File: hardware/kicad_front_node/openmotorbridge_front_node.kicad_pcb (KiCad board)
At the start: 2 copper layers, 82 x 50 mm, 58 parts, among them J1 12V_KL15_GND, J10 12V_QI_POWER, J11 12V_AUX_LIGHT, J12 QWIIC_I2C, J2 CAN_H_L_GND, J3 HANDLEBAR_MULTI_BTN, J4 USB_UPSTREAM_HOST, J5 USB_DN1_PHONE_PD20W, J5_MP3 USB_DN3_GLOVEBOX_PD20W, J6 USB_DN2_CP2AA_PIGTAIL, J6_AUX USB_DN4_COCKPIT_AUX, J7 USB-C_SERVICE, J8 ACTION_CAM_5V_PWR, J9 MIRROR_BSD_LEDS, K1 CPC1017N_CAN_RELAY, Q1 DMN63D8_BSD_MOSFET, Q2 TPS1H100_AUX_LIGHT, SW1 BOOT, SW2 RESET, U1 ESP32-S3-WROOM-1U, U2 USB2514Bi-AEZG, U3 TPS54302_5V_BUCK, U4 TPS2051B_PORT2_GATE, U5 SW3526_USB_PD1_20W, U6 TCAN334G_CAN, U7 TLV75533P_3V3_LDO, U8 SW3526_USB_PD3_20W, U9 DW3110, Y1 24.000MHz

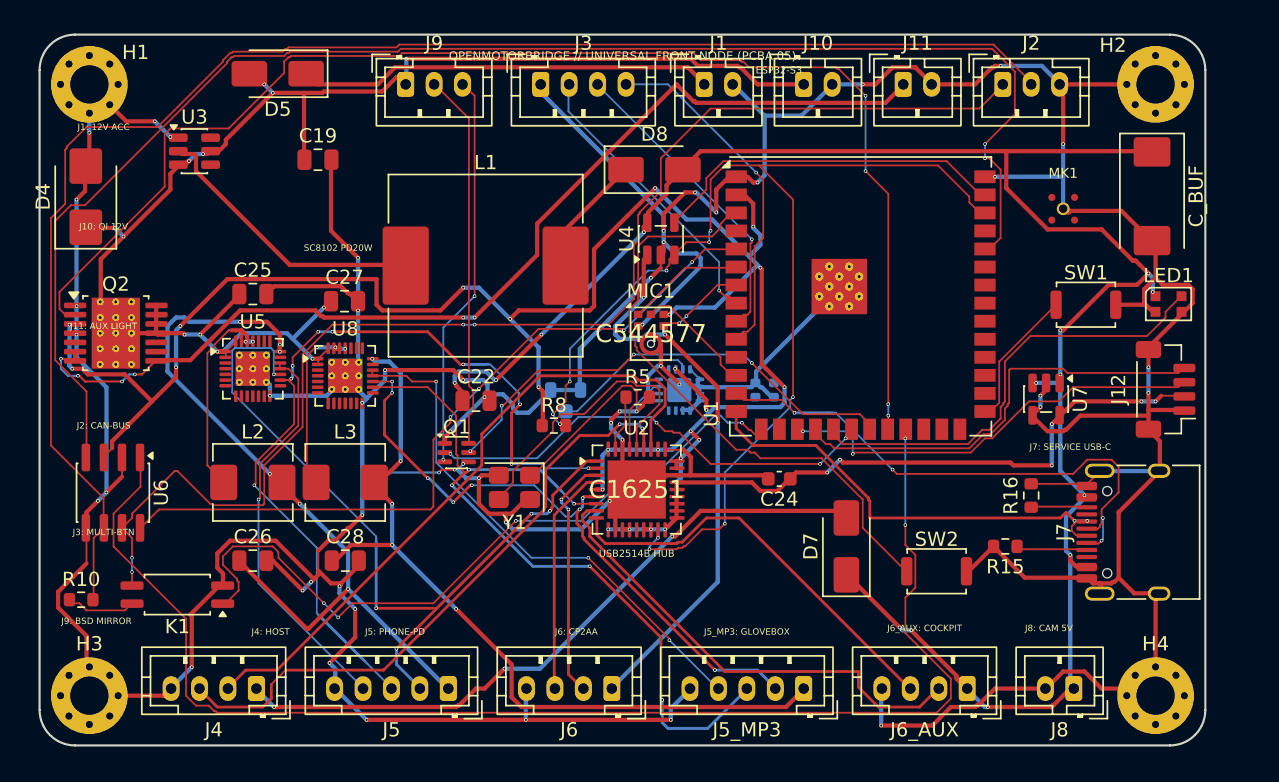
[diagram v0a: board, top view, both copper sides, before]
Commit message: fix(hardware): fleet-wide 7-PCBA remediation, schematic parity & doc alignment
- PCBA 01 (Central Box): Synchronized DTM-12 schematic and PCB routing, purged obsolete analog audio transformers/HD26 connector.
- PCBA 03 (Smart Cartridge): Verified Kelvin ground isolation on J_AUDIO_PWR, resolved U1.16 BAY_SELECT single net.
- PCBA 05 (Front Node): Mapped DW3110 UWB SPI/IRQ/RST to ESP32-S3 pads 30-35, connected MK1 I2S MEMS mic and Y_UWB crystal.
- PCBA 07 (Smart Keyfob): Connected 12 unrouted signals (SX1262 LoRa SPI, DRV2605L I2C, SWD, RTC crystal, buttons) to nRF52840 pads.
- PCBA 08 (Radar Sub-MCU): Synchronized J1.1 power rail to VCC_5V, connected Y1_UWB crystal to DW3110 pads 4 & 5.
- PCBA 09 & PCBA 10 (OMM 2.4 GHz & 446 MHz): Verified 4-layer stackup, BQ24075 ground ties, SA818 isolation, and vertical B.Cu J_HELMET orientation.
- Tools: Added verify_hardware_integrity.py with automated DRC/parity/single-net/floating-pad checks (all 7 PCBAs HEALTHY).
- Docs: Synchronized docs/de and docs/en hardware specifications, pinouts, and DTM-12 architecture.
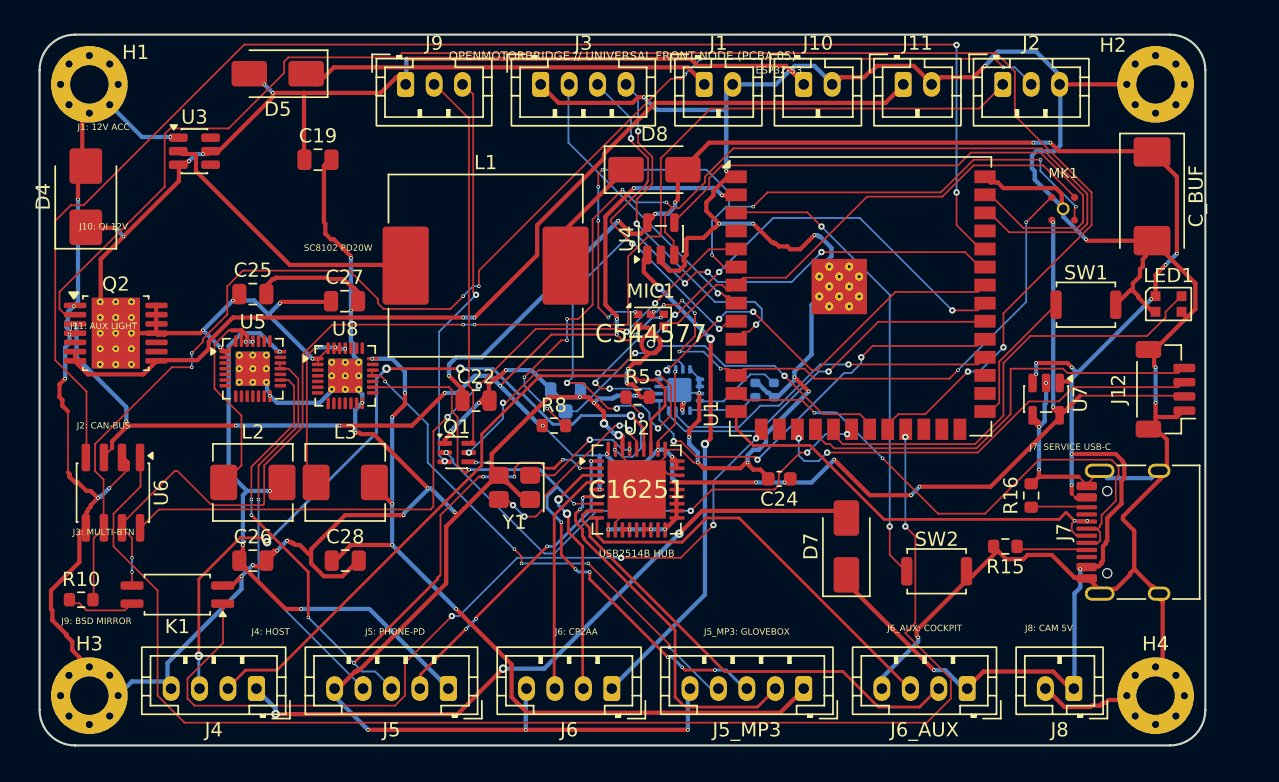
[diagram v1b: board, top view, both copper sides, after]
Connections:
- MK1 pad 1: (no net) -> MIC_I2S_DATA
- MK1 pad 2: (no net) -> MIC_I2S_BCLK
- MK1 pad 3: (no net) -> MIC_I2S_WS
- MK1 pad 4: (no net) -> VCC_3V3
- U1 pad 30: (no net) -> UWB_SCK
- U1 pad 31: (no net) -> UWB_MOSI
- U1 pad 32: (no net) -> UWB_MISO
- U1 pad 33: (no net) -> UWB_CS
- U1 pad 34: (no net) -> UWB_IRQ
- U1 pad 35: (no net) -> UWB_RST
- U1 pad 4: KL15_SENSE -> (no net)
- U2 pad 14: VDD12_HUB -> (no net)
- U3 pad 4: FB_BUCK -> (no net)
- U3 pad 6: BST_BUCK -> (no net)
- U9 pad 4: GND -> UWB_XTAL1
- U9 pad 5: GND -> UWB_XTAL2
- Y_UWB pad 1: (no net) -> UWB_XTAL1
- Y_UWB pad 3: (no net) -> UWB_XTAL2
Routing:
- net UWB_RST: track 0.00 -> 54.0 mm, vias 0 -> 7
- net MIC_I2S_WS: track 7.94 -> 58.5 mm, vias 0 -> 9
- net USB_DN1_DM: track 64.8 -> 21.8 mm, vias 5 -> 4
- net UWB_CS: track 0.00 -> 39.9 mm, vias 0 -> 5
- net MIC_I2S_DATA: track 7.95 -> 41.7 mm, vias 0 -> 8
- net MIC_I2S_BCLK: track 6.02 -> 34.9 mm, vias 2 -> 0
- net UWB_MOSI: track 0.00 -> 28.8 mm, vias 0 -> 3
- net UWB_IRQ: track 0.00 -> 28.3 mm, vias 0 -> 3
- net UWB_MISO: track 0.00 -> 26.4 mm, vias 0 -> 1
- net UWB_SCK: track 0.00 -> 24.5 mm, vias 0 -> 1
- net GND: track 465.5 -> 488.6 mm, vias 54 -> 55
- net AUX_LIGHT_EN: track 93.5 -> 114.8 mm, vias 4 -> 2
- net VCC_3V3: track 183.9 -> 164.1 mm, vias 31 -> 30
- net USB_DN3_DM: track 44.9 -> 26.2 mm, vias 8 -> 2
- net OTTOCAST_PWR_EN: track 24.8 -> 42.4 mm
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
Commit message: feat(hardware): achieve 100% 0-error DRC across all 7 official PCBAs and complete 4-layer Cartridge audio switching
- PCBA 01 (Central Box): Resolved keepout zone violation at U.FL ANT1, refilled zones (0 errors, 0 unconnected).
- PCBA 03 (Universal Smart Cartridge): Upgraded to 4 layers (JLC04161H), added SPDT analog/digital switch U4 (TS5A3159DBVR) on B.Cu and 10k pull-up R9 on F.Cu, routed symmetrical audio/OMM nets, schematic ERC 0 errors, DRC 0 errors, 0 unconnected.
- PCBA 05 (Front Node): 4-layer upgrade, solid GND plane, snapped OTTOCAST_FAULT_N (0 errors, 0 unconnected).
- PCBA 07 (Smart Keyfob): 4-layer upgrade, fixed Edge.Cuts arc alignment, routed U2 pad 23 (0 errors, 0 unconnected).
- PCBA 08 (Radar Sub-MCU), PCBA 09 (OMM 2.4 GHz), PCBA 10 (OMM 446 MHz): Verified 100% clean (0 errors, 0 unconnected).
- Added reproducibility tools: tools/sync_cartridge_sch.py and tools/remediate_pcba03.py.
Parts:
- moved Y1 4.21 mm to (129.4, 103.2), turned to 90 degrees
- turned U2 to 90 degrees
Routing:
- net GND: track 488.6 -> 100.6 mm, vias 55 -> 31
- net AUX_LIGHT_EN: track 114.8 -> 77.1 mm, vias 2 -> 6
- net CAN_L: track 94.4 -> 128.3 mm, vias 7 -> 3
- net USB_DN1_DM: track 21.8 -> 53.3 mm, vias 4 -> 1
- net UWB_RST: track 54.0 -> 29.3 mm, vias 7 -> 3
- net USB_DN3_DM: track 26.2 -> 49.4 mm, vias 2 -> 3
- net CAN_SILENT: track 53.3 -> 72.8 mm, vias 4 -> 2
- net MIC_I2S_WS: track 58.5 -> 40.2 mm, vias 9 -> 4
- net OTTOCAST_FAULT_N: track 72.5 -> 54.9 mm, vias 6 -> 7
- net USB_UP_DP: track 51.4 -> 34.1 mm, vias 5 -> 3
- net VCC_3V3: track 164.1 -> 149.0 mm, vias 30 -> 24
- net USB_UP_DM: track 46.3 -> 32.1 mm, vias 0 -> 1
- net CAN_TERM_EN: track 59.7 -> 45.5 mm, vias 4 -> 6
- net VCC_5V_OTTOCAST: track 35.5 -> 49.1 mm, vias 3 -> 0
- net UWB_CS: track 39.9 -> 27.5 mm, vias 5 -> 3
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- added copper zone on In1.Cu, net GND
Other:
- copper layers 2 -> 4

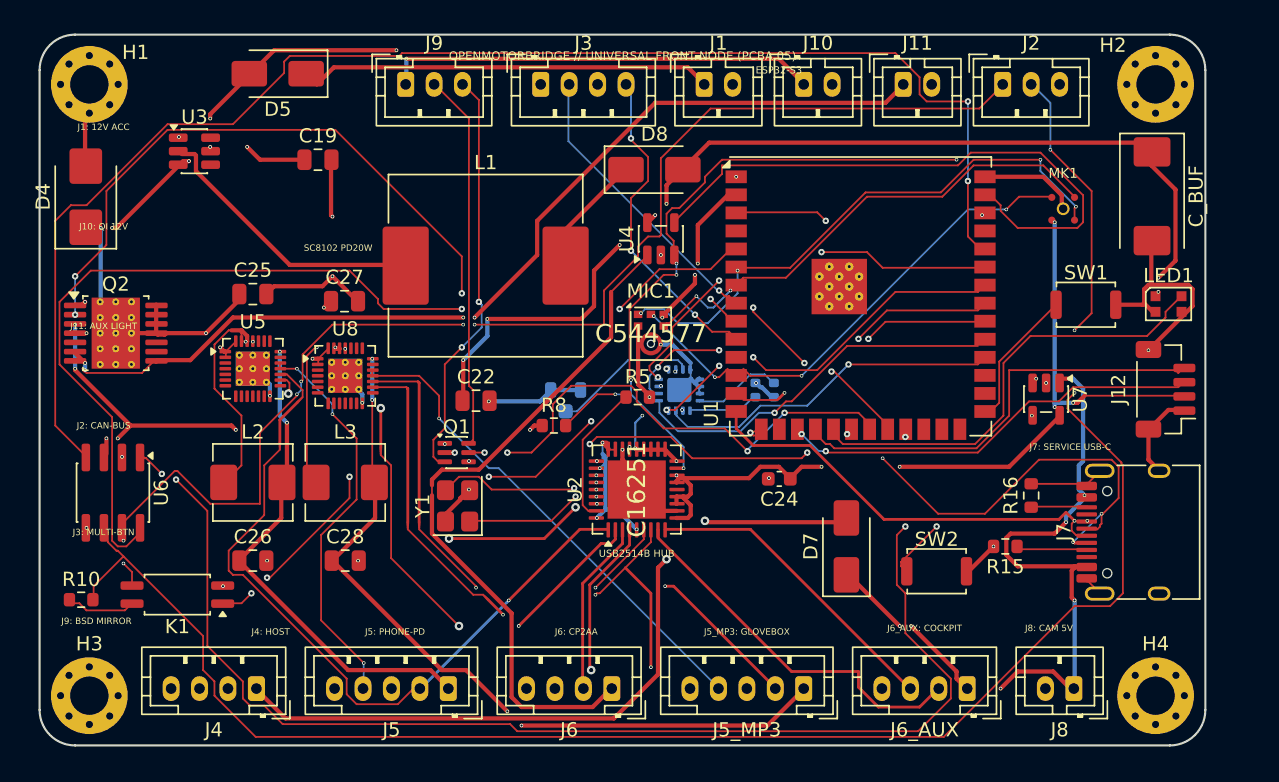
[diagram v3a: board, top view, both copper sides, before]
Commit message: feat(front-node): finalize dual-satellite architecture, CAD enclosures and smart-screen mode
- PCBA 05: Streamline board to 44 components with J_COCKPIT (16-pin) & J_VEHICLE (8-pin) dual-row headers, ESP32-S3 and DW3000 UWB.
- Enclosure: Update 00_front_node_tub.scad with continuous O-ring perimeter groove and circular Ø 8.0 mm TPU cable gland entries.
- Satellites: Implement cockpit_breakout_block.scad (5x USB-C, PTT, M3 clamp, dovetail) and vehicle_breakout_block.scad (4x COTS latching sockets).
- Use-Cases: Document 3 cockpit operating modes for RKS/naked cruisers including Mode C standalone smart-screen (Carpuride/Chigee) on [HOST].
- CAD & BOM: Re-render all Front Node 3D previews, register build targets in build_cad_from_openscad.py, and update doc chapters 07, 08, 15 & bom_catalog.js.
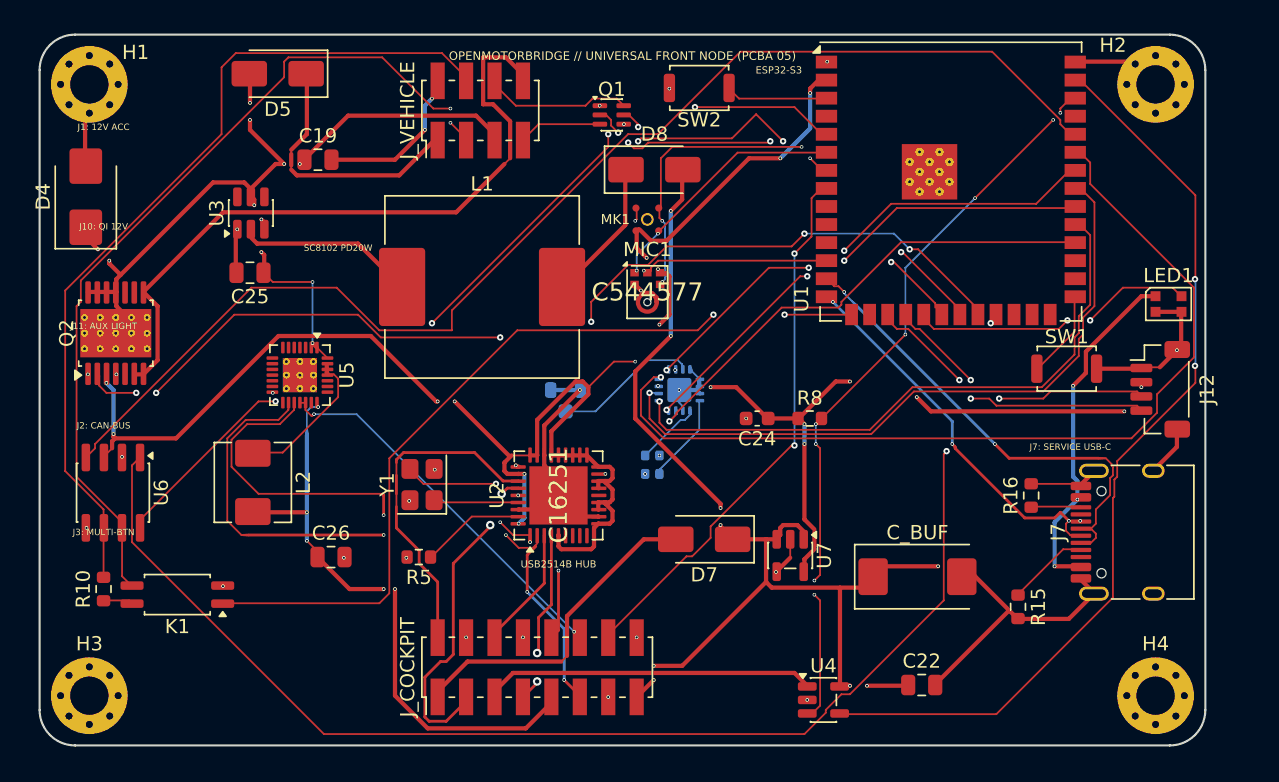
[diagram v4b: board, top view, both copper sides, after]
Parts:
- removed C27: 10uF_50V_PD3, C_0805_2012Metric
- removed C28: 22uF_25V_PD3, C_0805_2012Metric
- removed J1: 12V_KL15_GND, JST_PH_B2B-PH-K_1x02_P2.00mm_Vertical
- removed J10: 12V_QI_POWER, JST_PH_B2B-PH-K_1x02_P2.00mm_Vertical
- removed J11: 12V_AUX_LIGHT, JST_PH_B2B-PH-K_1x02_P2.00mm_Vertical
- removed J2: CAN_H_L_GND, JST_PH_B3B-PH-K_1x03_P2.00mm_Vertical
- removed J3: HANDLEBAR_MULTI_BTN, JST_PH_B4B-PH-K_1x04_P2.00mm_Vertical
- removed J4: USB_UPSTREAM_HOST, JST_PH_B4B-PH-K_1x04_P2.00mm_Vertical
- removed J5: USB_DN1_PHONE_PD20W, JST_PH_B5B-PH-K_1x05_P2.00mm_Vertical
- removed J5_MP3: USB_DN3_GLOVEBOX_PD20W, JST_PH_B5B-PH-K_1x05_P2.00mm_Vertical
- removed J6: USB_DN2_CP2AA_PIGTAIL, JST_PH_B4B-PH-K_1x04_P2.00mm_Vertical
- removed J6_AUX: USB_DN4_COCKPIT_AUX, JST_PH_B4B-PH-K_1x04_P2.00mm_Vertical
- removed J8: ACTION_CAM_5V_PWR, JST_PH_B2B-PH-K_1x02_P2.00mm_Vertical
- removed J9: MIRROR_BSD_LEDS, JST_PH_B3B-PH-K_1x03_P2.00mm_Vertical
- removed L3: 4.7uH_PD3_Choke, L_Sunlord_MWSA0503S
- removed U8: SW3526_USB_PD3_20W, QFN-28-1EP_4x4mm_P0.4mm_EP2.4x2.4mm_ThermalVias
- added J_COCKPIT: COCKPIT_16P_SMD, PinHeader_2x08_P2.00mm_Vertical_SMD, F.Cu at (135.0, 114.5)
- added J_VEHICLE: VEHICLE_8P_SMD, PinHeader_2x04_P2.00mm_Vertical_SMD, F.Cu at (131.0, 75.3)
- moved SW2 37.9 mm to (146.4, 73.8), turned to 180 degrees
- moved C22 37.2 mm to (162.1, 115.8)
- moved U4 34.4 mm to (155.1, 116.8), turned to 0 degrees
- moved C_BUF 31.4 mm to (161.8, 108.1), turned to 0 degrees
- moved MK1 29.3 mm to (142.8, 83.0)
- moved Q1 26.1 mm to (140.2, 75.7)
- moved U7 21.1 mm to (152.8, 106.6)
- moved R5 19.1 mm to (126.7, 106.8), turned to 180 degrees
- moved R8 18.0 mm to (154.2, 97.0)
- moved U1 10.3 mm to (164.1, 80.3)
- moved D7 10.0 mm to (146.8, 105.5), turned to 180 degrees
- moved Y_UWB 9.49 mm to (143.1, 100.2), turned to 90 degrees
- moved U3 5.89 mm to (114.9, 82.5), turned to 90 degrees
- moved U2 5.52 mm to (136.5, 102.4)
- moved C26 5.51 mm to (120.5, 106.8)
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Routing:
- net CAN_L: track 128.3 -> 60.2 mm, vias 3 -> 0
- net VBUS_PD3_OUT: track 54.7 -> 0.00 mm, vias 4 -> 0
- net USB_DN3_DP: track 50.3 -> 0.00 mm, vias 3 -> 0
- net USB_DN3_DM: track 49.4 -> 0.00 mm, vias 3 -> 0
- net UWB_RST: track 29.3 -> 64.6 mm, vias 3 -> 1
- net USB_DN3_CC: track 34.9 -> 0.00 mm, vias 1 -> 0
- net +12V_PROT: track 100.8 -> 68.1 mm, vias 12 -> 11
- net USB_UP_VBUS: track 52.7 -> 23.3 mm, vias 2 -> 0
- net CAN_H: track 89.9 -> 60.7 mm, vias 6 -> 2
- net ESP_EN: track 35.8 -> 7.30 mm, vias 2 -> 0
- net VCC_5V: track 138.4 -> 110.8 mm, vias 15 -> 12
- net USB_DN4_DM: track 26.4 -> 0.00 mm
- net VCC_5V_OTTOCAST: track 49.1 -> 23.4 mm
- net BSD_RIGHT_N: track 29.1 -> 5.86 mm, vias 2 -> 0
- net PTT_IN3_N: track 22.8 -> 0.00 mm, vias 3 -> 0
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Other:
- board text removed: "J4: HOST"
- board text removed: "J5: PHONE-PD"
- board text removed: "J5_MP3: GLOVEBOX"
- board text removed: "J6: CP2AA"
- board text removed: "J6_AUX: COCKPIT"
- board text removed: "J8: CAM 5V"
- board text removed: "J9: BSD MIRROR"

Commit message: feat(front-node): integrate I2C bus into J_VEHICLE 12-pin, pass prefab-gate & update cad packages
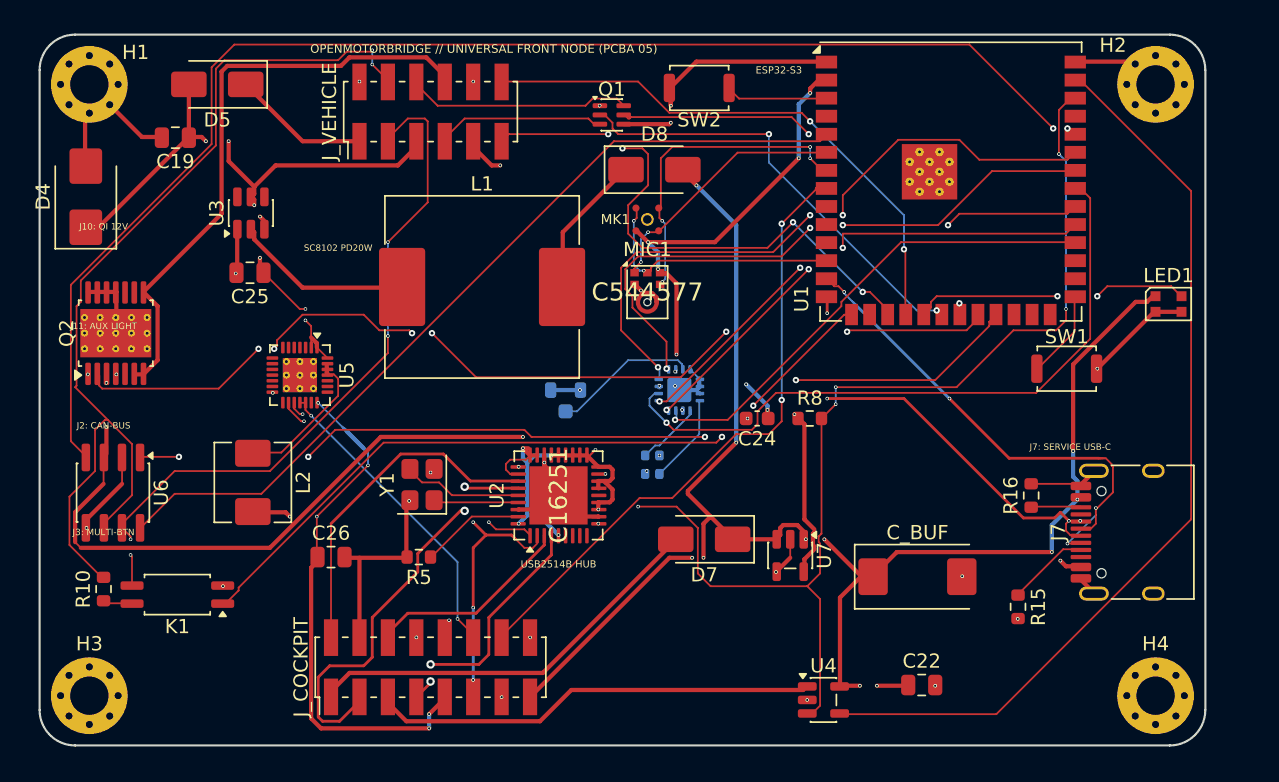
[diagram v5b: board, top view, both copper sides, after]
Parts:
- removed J12: QWIIC_I2C, JST_SH_BM04B-SRSS-TB_1x04-1MP_P1.00mm_Vertical
- removed the J_VEHICLE at (131.0, 75.3)
- added J_VEHICLE: VEHICLE_12P_SMD, PinHeader_2x06_P2.00mm_Vertical_SMD, F.Cu at (127.5, 75.4)
- moved C19 10.1 mm to (109.5, 77.2), turned to 180 degrees
- moved J_COCKPIT 7.50 mm to (127.5, 114.5)
- moved D5 4.32 mm to (112.5, 73.5)
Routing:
- net TWAI_TX: track 94.7 -> 65.0 mm, vias 2 -> 4
- net I2C_SCL: track 20.4 -> 39.3 mm
- net I2C_SDA: track 20.9 -> 39.6 mm, vias 2 -> 4
- net UWB_RST: track 64.6 -> 46.3 mm, vias 1 -> 3
- net VCC_3V3: track 169.7 -> 154.2 mm
- net USB_DN1_DP: track 46.6 -> 33.9 mm
- net CAN_H: track 60.7 -> 49.5 mm, vias 2 -> 4
- net OTTOCAST_FAULT_N: track 68.3 -> 79.4 mm, vias 9 -> 6
- net USB_DN1_DM: track 39.7 -> 30.5 mm, vias 4 -> 3
- net KL15_12V_SW: track 18.7 -> 9.66 mm
- net TWAI_RX: track 87.5 -> 96.0 mm, vias 0 -> 2
- net UWB_MOSI: track 43.4 -> 35.0 mm, vias 1 -> 3
- net UWB_IRQ: track 34.6 -> 42.9 mm
- net VCC_5V_OTTOCAST: track 23.4 -> 31.5 mm
- net +12V_AUX: track 49.1 -> 42.2 mm
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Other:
- board text removed: "J1: 12V ACC"
